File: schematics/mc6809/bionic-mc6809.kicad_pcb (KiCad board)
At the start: 2 copper layers, 27.9 x 68.6 mm, 9 parts, among them J1 Bionic-P135, J2 Bionic-P245, U1 MC6809P, U2 11AA010-I/TT

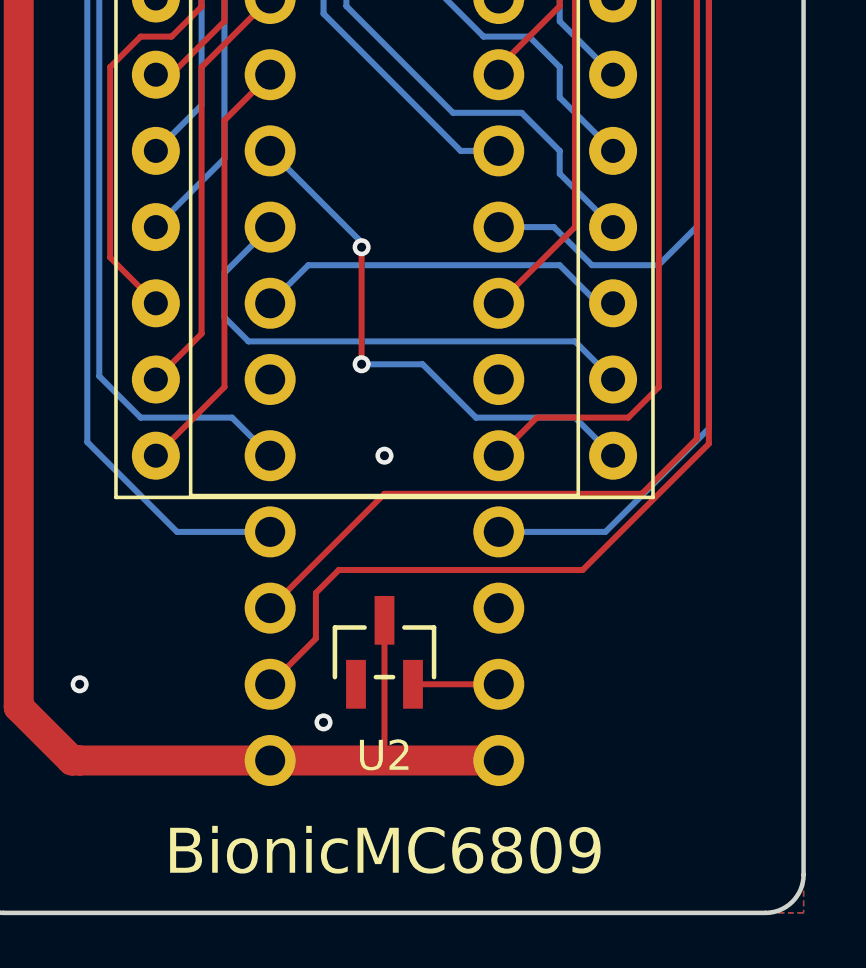
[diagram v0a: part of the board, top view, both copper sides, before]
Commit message: [MC6809] Fix EEPROM pinout
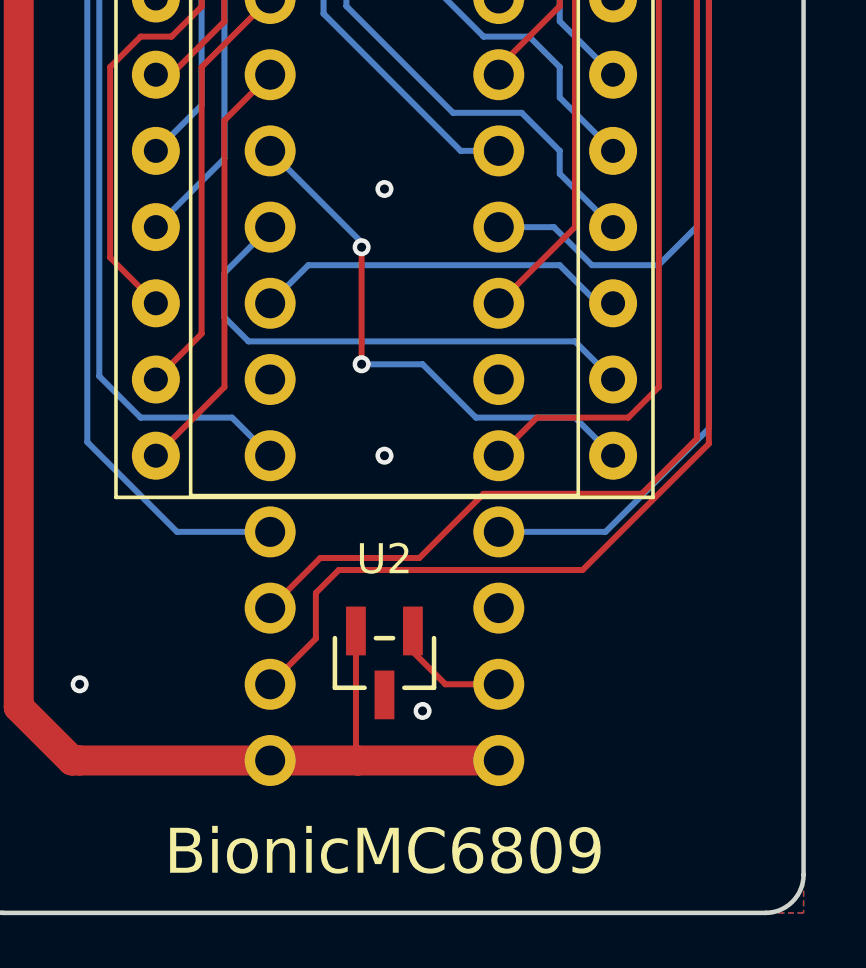
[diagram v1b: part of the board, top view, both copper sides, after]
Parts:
- moved U2 0.35 mm to (115.0, 130.2), turned to 180 degrees
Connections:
- U2 pad 1: GND -> Net-(J2-P57)
- U2 pad 2: Net-(J2-P57) -> VCC
- U2 pad 3: VCC -> GND
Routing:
- net Net-(J2-P57): track 2.86 -> 4.00 mm
- net GND: vias 3 -> 4
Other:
- board text added: "Rev. 6"
- board text removed: "Rev. 5"
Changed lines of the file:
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@@
   (title_block
     (title "BionicMC6809")
-    (date "2024-05-04")
-    (rev "5")
+    (date "2024-11-01")
+    (rev "6")
     (company "Tadashi G. Takaoka")
   )
@@
   )
   (footprint "0-LocalLibrary:SOT-23_MC_MCH-M" (layer "F.Cu")
-    (at 114.97 129.894)
+    (at 114.97 130.248 180)
     (descr "Microchip 11AAxxx-I/TT UNI/O 1Kbit Serial EEPROM")
     (property "Sheetfile" "bionic-mc6809.kicad_sch")
@@
         (effects (font (size 1 1) (thickness 0.15)))
     )
-    (fp_text value "11AA010-I/TT" (at 0 0 unlocked) (layer "F.Fab")
+    (fp_text value "11AA010-I/TT" (at 0 0 180 unlocked) (layer "F.Fab")
         (effects (font (size 1 1) (thickness 0.15)))
     )
-    (fp_text user "${REFERENCE}" (at 0 0 unlocked) (layer "F.Fab")
+    (fp_text user "${REFERENCE}" (at 0 0 180 unlocked) (layer "F.Fab")
         (effects (font (size 1 1) (thickness 0.15)))
     )
@@
     (fp_circle (center -1.270999 0.446) (end -1.143999 0.446)
       (stroke (width 0.0254) (type solid)) (fill none) (layer "F.Fab"))
-    (pad "1" smd rect (at -0.950001 1.066) (size 0.6604 1.6256) (layers "F.Cu" "F.Paste" "F.Mask")
+    (pad "1" smd rect (at -0.950001 1.066 180) (size 0.6604 1.6256) (layers "F.Cu" "F.Paste" "F.Mask")
+      (net 26 "Net-(J2-P57)") (pinfunction "SCIO") (pintype "bidirectional"))
+    (pad "2" smd rect (at 0.950001 1.066 180) (size 0.6604 1.6256) (layers "F.Cu" "F.Paste" "F.Mask")
+      (net 1 "VCC") (pinfunction "VCC") (pintype "power_in"))
+    (pad "3" smd rect (at 0 -1.066 180) (size 0.6604 1.6256) (layers "F.Cu" "F.Paste" "F.Mask")
       (net 2 "GND") (pinfunction "VSS") (pintype "power_in"))
-    (pad "2" smd rect (at 0.950001 1.066) (size 0.6604 1.6256) (layers "F.Cu" "F.Paste" "F.Mask")
-      (net 26 "Net-(J2-P57)") (pinfunction "SCIO") (pintype "bidirectional"))
-    (pad "3" smd rect (at 0 -1.066) (size 0.6604 1.6256) (layers "F.Cu" "F.Paste" "F.Mask")
-      (net 1 "VCC") (pinfunction "VCC") (pintype "power_in"))
     (model "${KIPRJMOD}/0-LocalLibrary/SOT-23_MC_MCH.step"
       (offset (xyz 0 0 0))
@@
     (effects (font (size 0.8 0.8)) (justify bottom mirror))
   )
-  (gr_text "Rev. 5" (at 107.096 136.802) (layer "B.SilkS")
+  (gr_text "Rev. 6" (at 107.096 136.802) (layer "B.SilkS")
     (effects (font (size 1 1)) (justify left mirror))
   )
@@
   (segment (start 114.1953 81.9507) (end 112.176 83.97) (width 0.2) (layer "F.Cu") (net 1))
   (segment (start 104.645 90.32) (end 104.556 90.231) (width 0.2) (layer "F.Cu") (net 1))
+  (segment (start 114.019999 133.438999) (end 114.081 133.5) (width 0.2) (layer "F.Cu") (net 1))
+  (segment (start 114.081 133.5) (end 111.16 133.5) (width 1) (layer "F.Cu") (net 1))
   (segment locked (start 111.16 133.5) (end 104.81 133.5) (width 1) (layer "F.Cu") (net 1))
   (segment (start 104.556 133.5) (end 102.778 131.722) (width 1) (layer "F.Cu") (net 1))
-  (segment locked (start 118.78 133.5) (end 111.16 133.5) (width 1) (layer "F.Cu") (net 1))
   (segment (start 114.1953 71.778) (end 114.1953 81.9507) (width 0.2) (layer "F.Cu") (net 1))
   (segment (start 112.176 83.97) (end 110.398 83.97) (width 0.2) (layer "F.Cu") (net 1))
@@
   (segment (start 102.778 131.722) (end 102.778 90.828) (width 1) (layer "F.Cu") (net 1))
   (segment (start 104.556 90.231) (end 104.556 90.1665) (width 0.2) (layer "F.Cu") (net 1))
+  (segment (start 118.78 133.5) (end 114.081 133.5) (width 1) (layer "F.Cu") (net 1))
+  (segment (start 114.019999 129.182) (end 114.019999 133.438999) (width 0.2) (layer "F.Cu") (net 1))
   (segment (start 102.778 90.828) (end 103.286 90.32) (width 1) (layer "F.Cu") (net 1))
-  (segment (start 114.97 133.5) (end 114.97 128.828) (width 0.2) (layer "F.Cu") (net 1))
   (segment (start 110.398 83.97) (end 108.836 85.532) (width 0.2) (layer "F.Cu") (net 1))
   (segment (start 108.836 88.834) (end 107.35 90.32) (width 0.2) (layer "F.Cu") (net 1))
   (via (at 104.81 130.96) (size 0.6) (drill 0.3) (layers "F.Cu" "B.Cu") (free) (net 2))
   (via (at 114.97 123.34) (size 0.6) (drill 0.3) (layers "F.Cu" "B.Cu") (free) (net 2))
-  (via (at 112.938 132.23) (size 0.6) (drill 0.3) (layers "F.Cu" "B.Cu") (free) (net 2))
+  (via (at 114.97 114.45) (size 0.6) (drill 0.3) (layers "F.Cu" "B.Cu") (free) (net 2))
+  (via (at 116.24 131.849) (size 0.6) (drill 0.3) (layers "F.Cu" "B.Cu") (free) (net 2))
   (segment (start 117.6135 71.778) (end 115.7447 71.778) (width 0.2) (layer "F.Cu") (net 3))
   (segment (start 109.382 79.398) (end 109.382 80.414) (width 0.2) (layer "B.Cu") (net 4))
@@
   (segment (start 105.064 79.906) (end 107.35 77.62) (width 0.2) (layer "B.Cu") (net 23))
   (segment (start 105.064 122.8858) (end 105.064 79.906) (width 0.2) (layer "B.Cu") (net 23))
-  (segment (start 123.548314 124.61) (end 114.97 124.61) (width 0.2) (layer "F.Cu") (net 24))
-  (segment (start 114.97 124.61) (end 111.16 128.42) (width 0.2) (layer "F.Cu") (net 24))
+  (segment (start 118.272 124.61) (end 116.132 126.75) (width 0.2) (layer "F.Cu") (net 24))
+  (segment (start 112.83 126.75) (end 111.16 128.42) (width 0.2) (layer "F.Cu") (net 24))
+  (segment (start 123.548314 124.61) (end 118.272 124.61) (width 0.2) (layer "F.Cu") (net 24))
+  (segment (start 116.132 126.75) (end 112.83 126.75) (width 0.2) (layer "F.Cu") (net 24))
+  (segment (start 125.384 122.774314) (end 123.548314 124.61) (width 0.2) (layer "F.Cu") (net 24))
   (segment (start 125.384 88.034) (end 125.384 122.774314) (width 0.2) (layer "F.Cu") (net 24))
   (segment (start 122.59 85.24) (end 125.384 88.034) (width 0.2) (layer "F.Cu") (net 24))
-  (segment (start 125.384 122.774314) (end 123.548314 124.61) (width 0.2) (layer "F.Cu") (net 24))
   (segment (start 125.784 85.894) (end 122.59 82.7) (width 0.2) (layer "F.Cu") (net 25))
   (segment (start 112.684 127.912) (end 113.446 127.15) (width 0.2) (layer "F.Cu") (net 25))
@@
   (segment (start 121.574 127.15) (end 125.784 122.94) (width 0.2) (layer "F.Cu") (net 25))
   (segment (start 111.16 130.96) (end 112.684 129.436) (width 0.2) (layer "F.Cu") (net 25))
-  (segment (start 118.78 130.96) (end 115.92 130.96) (width 0.2) (layer "F.Cu") (net 26))
+  (segment (start 115.920001 129.878001) (end 117.002 130.96) (width 0.2) (layer "F.Cu") (net 26))
+  (segment (start 117.002 130.96) (end 118.78 130.96) (width 0.2) (layer "F.Cu") (net 26))
+  (segment (start 115.920001 129.182) (end 115.920001 129.878001) (width 0.2) (layer "F.Cu") (net 26))
   (segment (start 122.336 125.88) (end 118.78 125.88) (width 0.2) (layer "B.Cu") (net 28))
   (segment (start 125.784 122.432) (end 122.336 125.88) (width 0.2) (layer "B.Cu") (net 28))

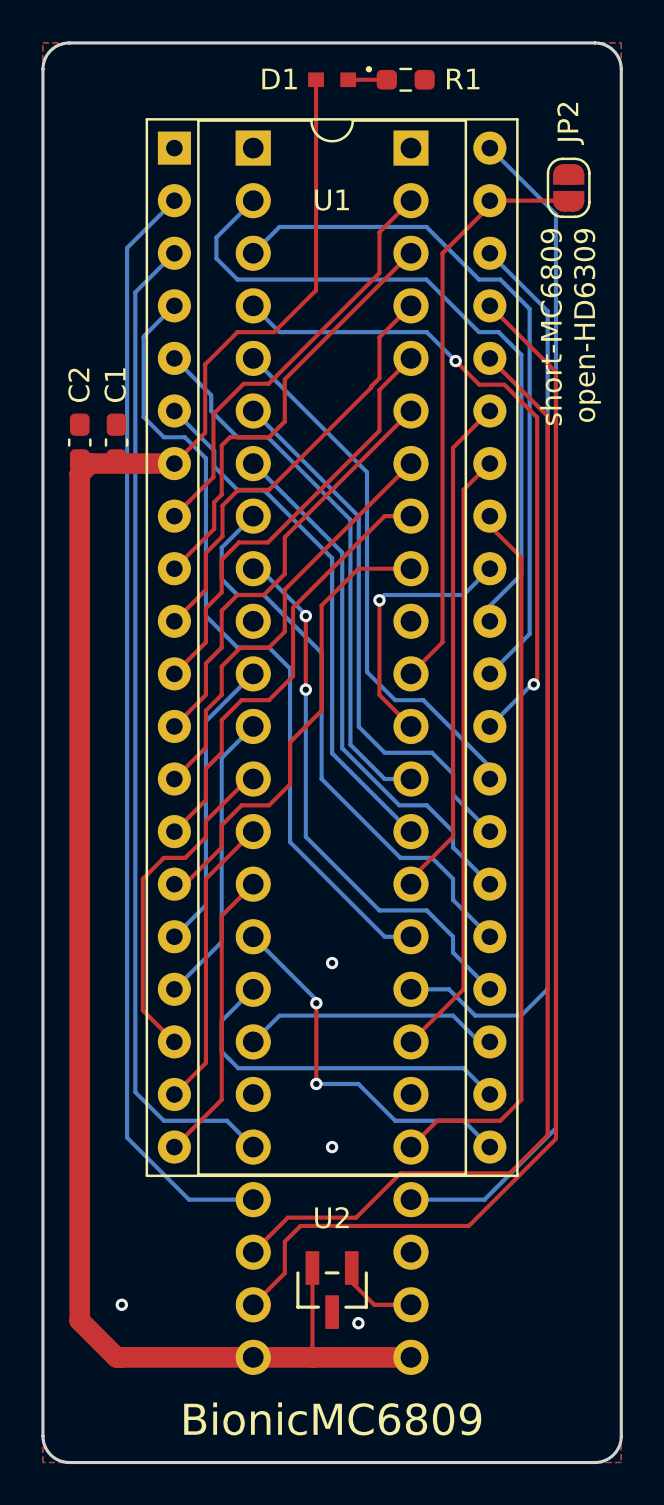
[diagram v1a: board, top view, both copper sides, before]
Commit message: [MC6809] Shrink board size
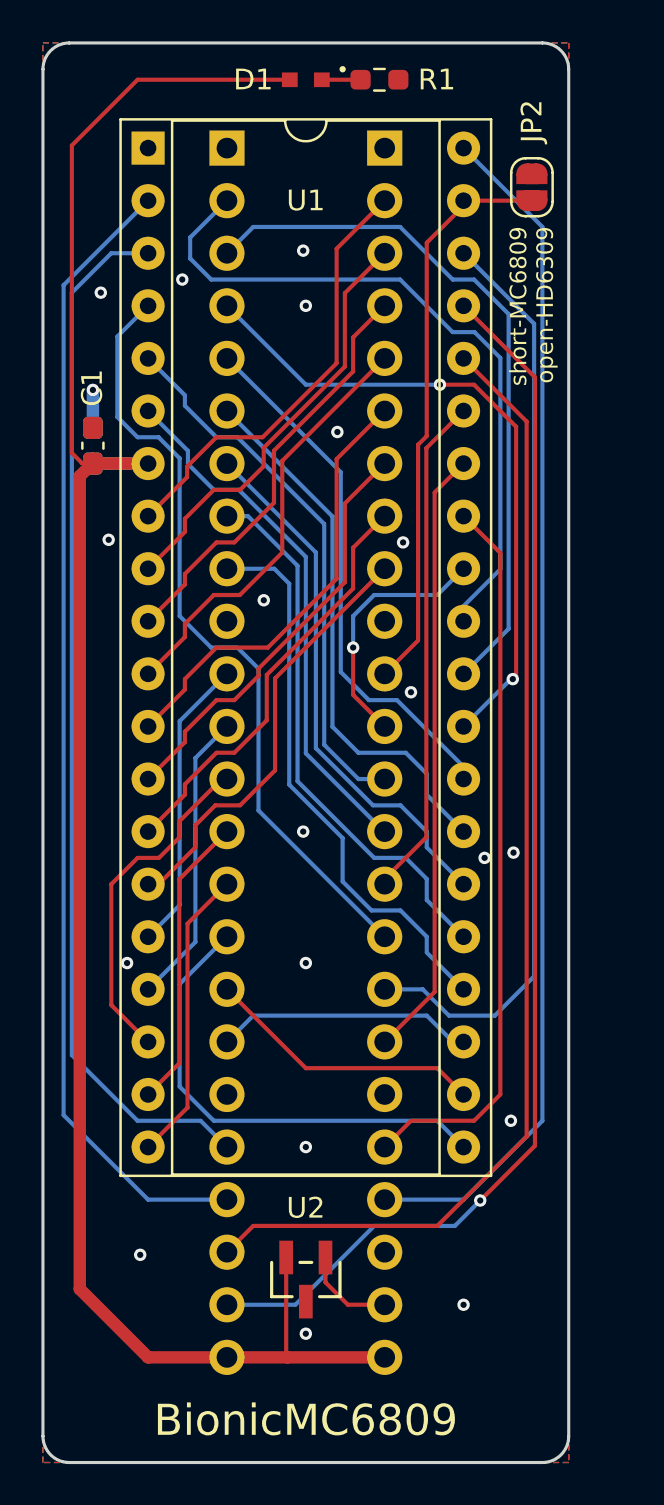
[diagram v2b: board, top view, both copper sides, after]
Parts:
- C2: moved to B.Cu
- moved JP2 1.78 mm to (124.6, 77.0)
- moved U2 1.37 mm to (113.7, 129.7)
- moved D1 1.27 mm to (113.7, 71.8)
- moved J1 1.27 mm to (109.9, 75.1)
- moved J2 1.27 mm to (117.5, 75.1)
- moved R1 1.27 mm to (117.3, 71.8)
- moved U1 1.27 mm to (106.1, 75.1)
- moved C1 1.15 mm to (103.4, 89.5)
- moved C2 0.65 mm to (103.4, 89.5)
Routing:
- net /P35: track 18.0 -> 23.1 mm, vias 2 -> 0
- net VCC: track 89.4 -> 94.1 mm
- net /P36: track 17.5 -> 13.5 mm
- net /P50: track 48.1 -> 50.6 mm
- net /P51: track 53.5 -> 55.5 mm
- net GND: track 0.00 -> 1.80 mm, vias 4 -> 20
- net /P27: track 22.5 -> 21.0 mm
- net /P16: track 28.0 -> 26.5 mm
- net /P26: track 21.5 -> 20.5 mm
- net /P45: track 38.7 -> 37.8 mm
- net /P24: track 20.7 -> 21.4 mm
- net /P55: track 57.1 -> 57.8 mm
- net /P17: track 26.6 -> 27.2 mm, vias 2 -> 0
- net /P20: track 20.7 -> 21.3 mm
- net /P46: track 44.4 -> 44.9 mm
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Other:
- board size 27.9 x 68.6 mm -> 25.4 x 68.6 mm

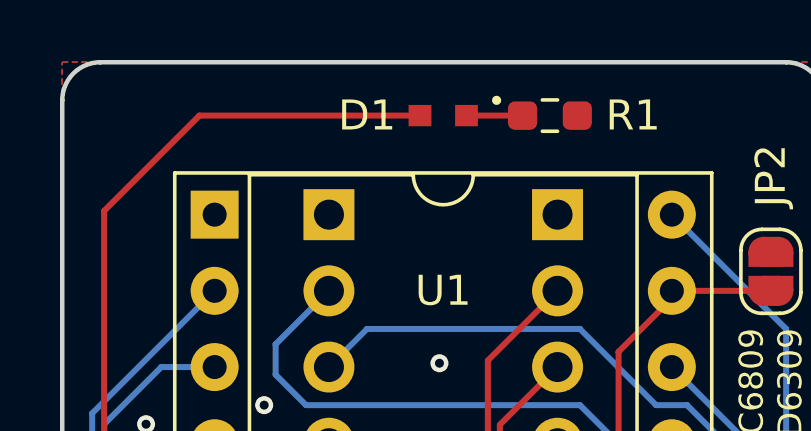
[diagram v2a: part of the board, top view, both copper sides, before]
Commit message: [schematics] Update LED footprint
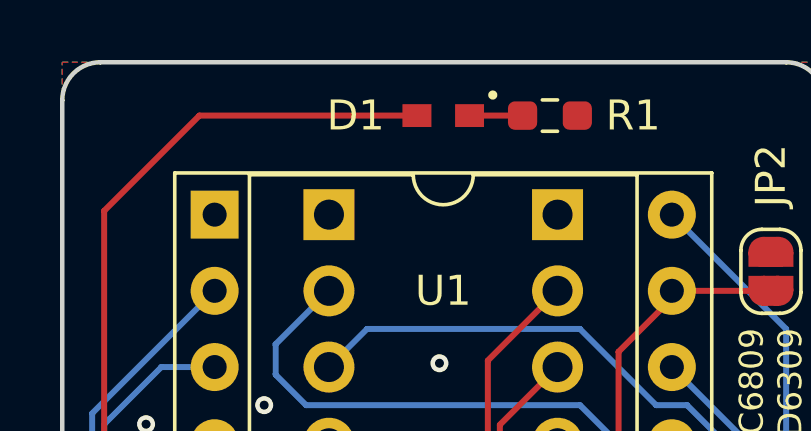
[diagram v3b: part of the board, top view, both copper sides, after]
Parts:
- D1: footprint 0-LocalLibrary:LED_CSL1901UW1_ROM -> 0-LocalLibrary:LED_CSL1901UW1_ROM-M

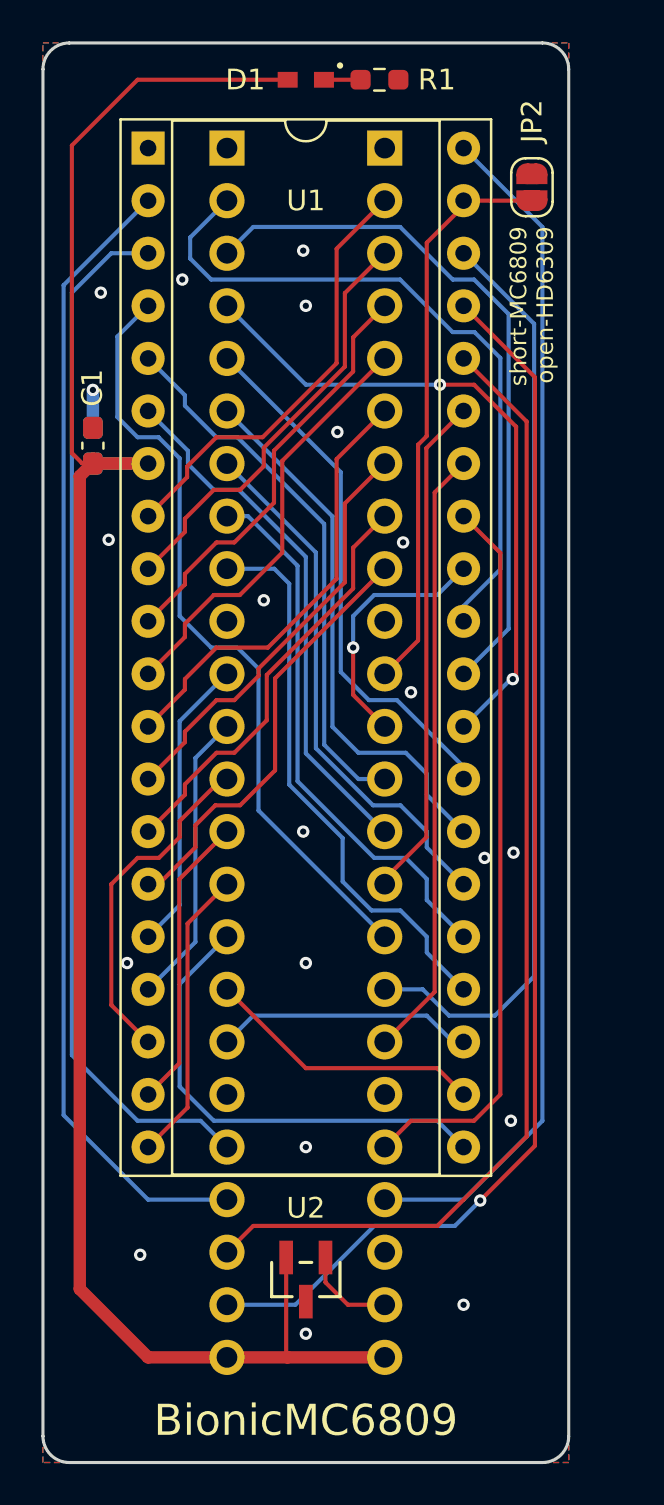
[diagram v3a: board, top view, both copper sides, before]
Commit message: [MC6809] Cleanup schematics
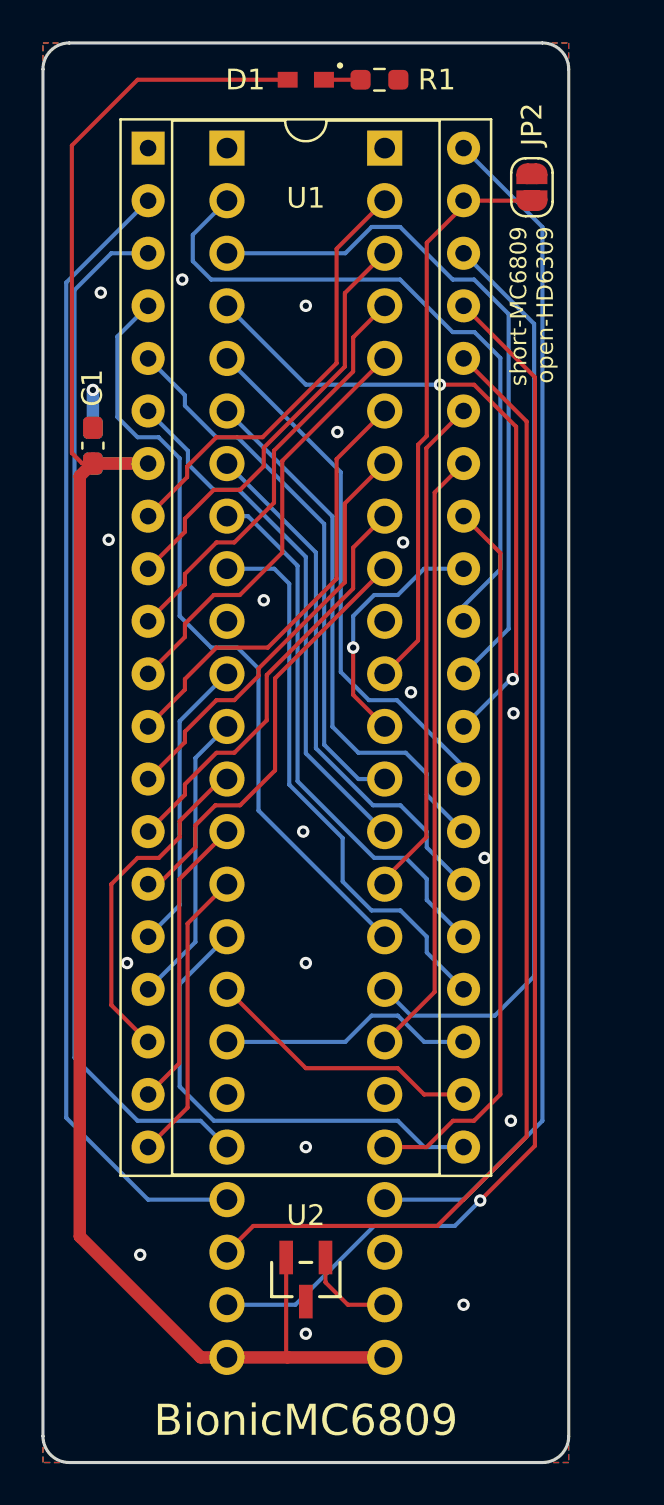
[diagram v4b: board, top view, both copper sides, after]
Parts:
- D1: footprint 0-LocalLibrary:LED_CSL1901UW1_ROM-M -> rhom:LED_CSL1901UW1_ROM-M
- J1: footprint 0-LocalLibrary:Bionic-P135_Vertical -> bionic:Bionic-P135_Vertical
- J2: footprint 0-LocalLibrary:Bionic-P245_Vertical -> bionic:Bionic-P245_Vertical
- JP2: footprint 0-LocalLibrary:SolderJumper-2_P1.3mm_Open_RoundedPad1.0x1.5mm -> bionic:SolderJumper-2_P1.3mm_Open_RoundedPad1.0x1.5mm
- U1: footprint 0-LocalLibrary:DIP-40_W15.24mm_Socket -> bionic:DIP-40_W15.24mm_Socket
- U2: footprint 0-LocalLibrary:SOT-23_MC_MCH-M -> microchip:SOT-23_MC_MCH-M
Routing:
- net VCC: track 94.0 -> 92.5 mm
- net GND: vias 20 -> 19
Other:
- rule pad_to_mask_clearance: 0.051 -> 0
